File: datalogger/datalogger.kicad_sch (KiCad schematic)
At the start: 42 parts, among them J1 MSD-1-A, J2 USB4216-03-A_REVA, Q1 NPN, Q2 NPN, U1 BME280, U2 CP2102N-Axx-xQFN28, U3 ESP32-C3-MINI-1-N4, U4 TLV76133DCYR

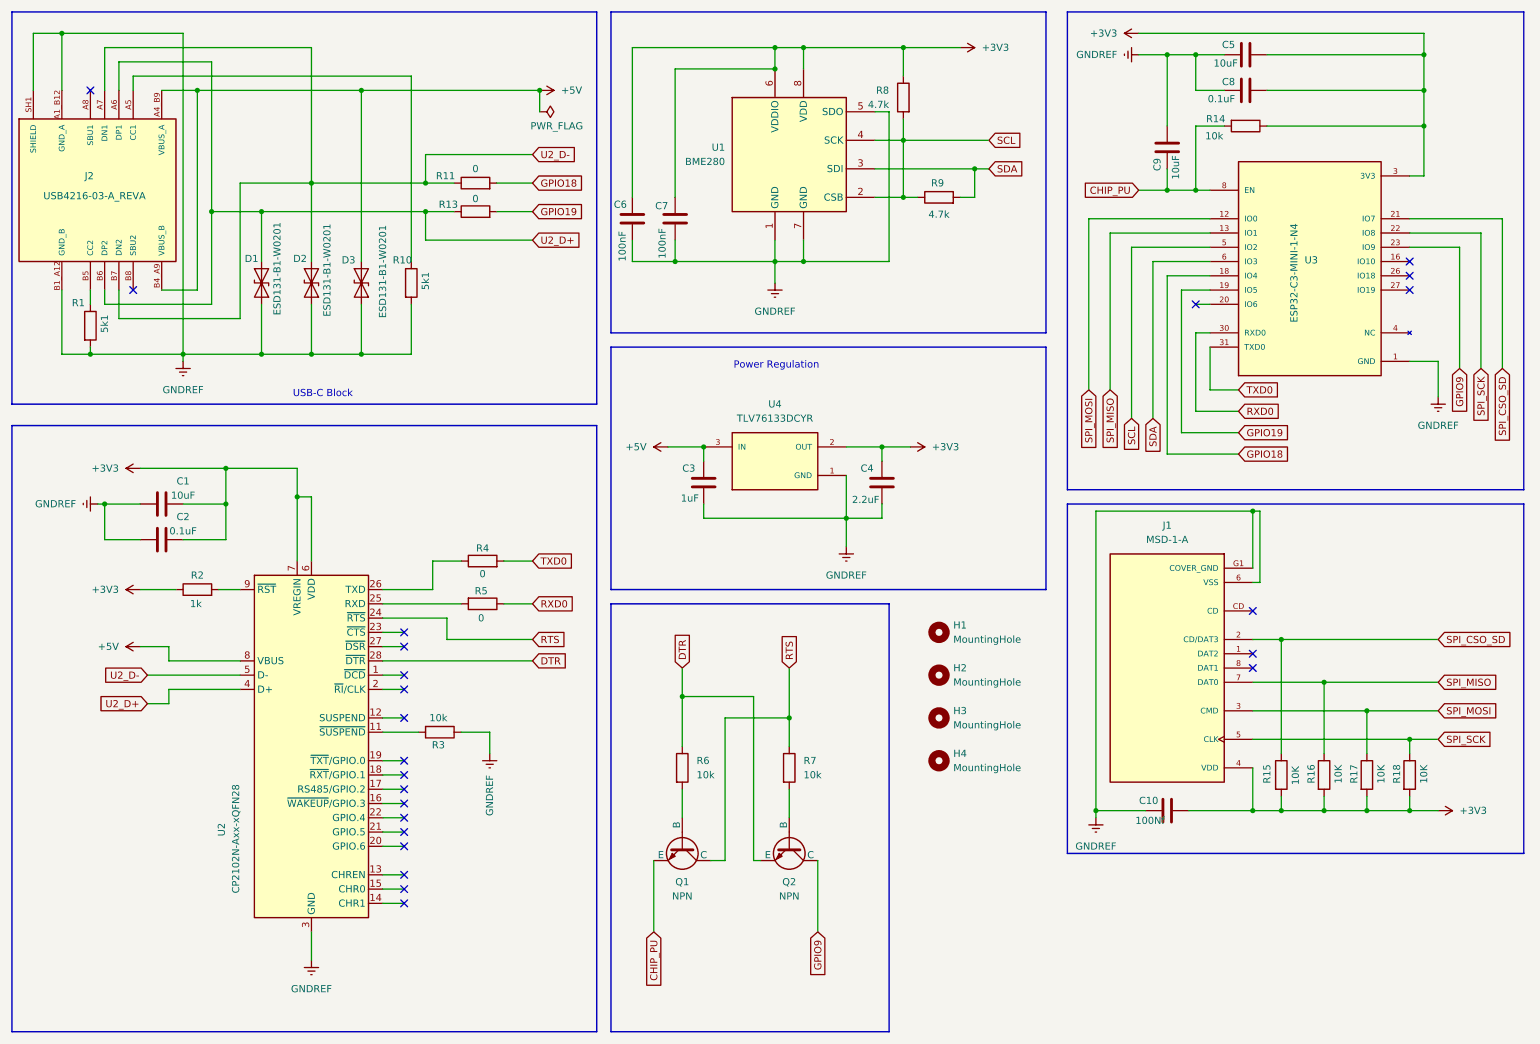
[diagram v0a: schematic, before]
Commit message: Change USB-C orientation
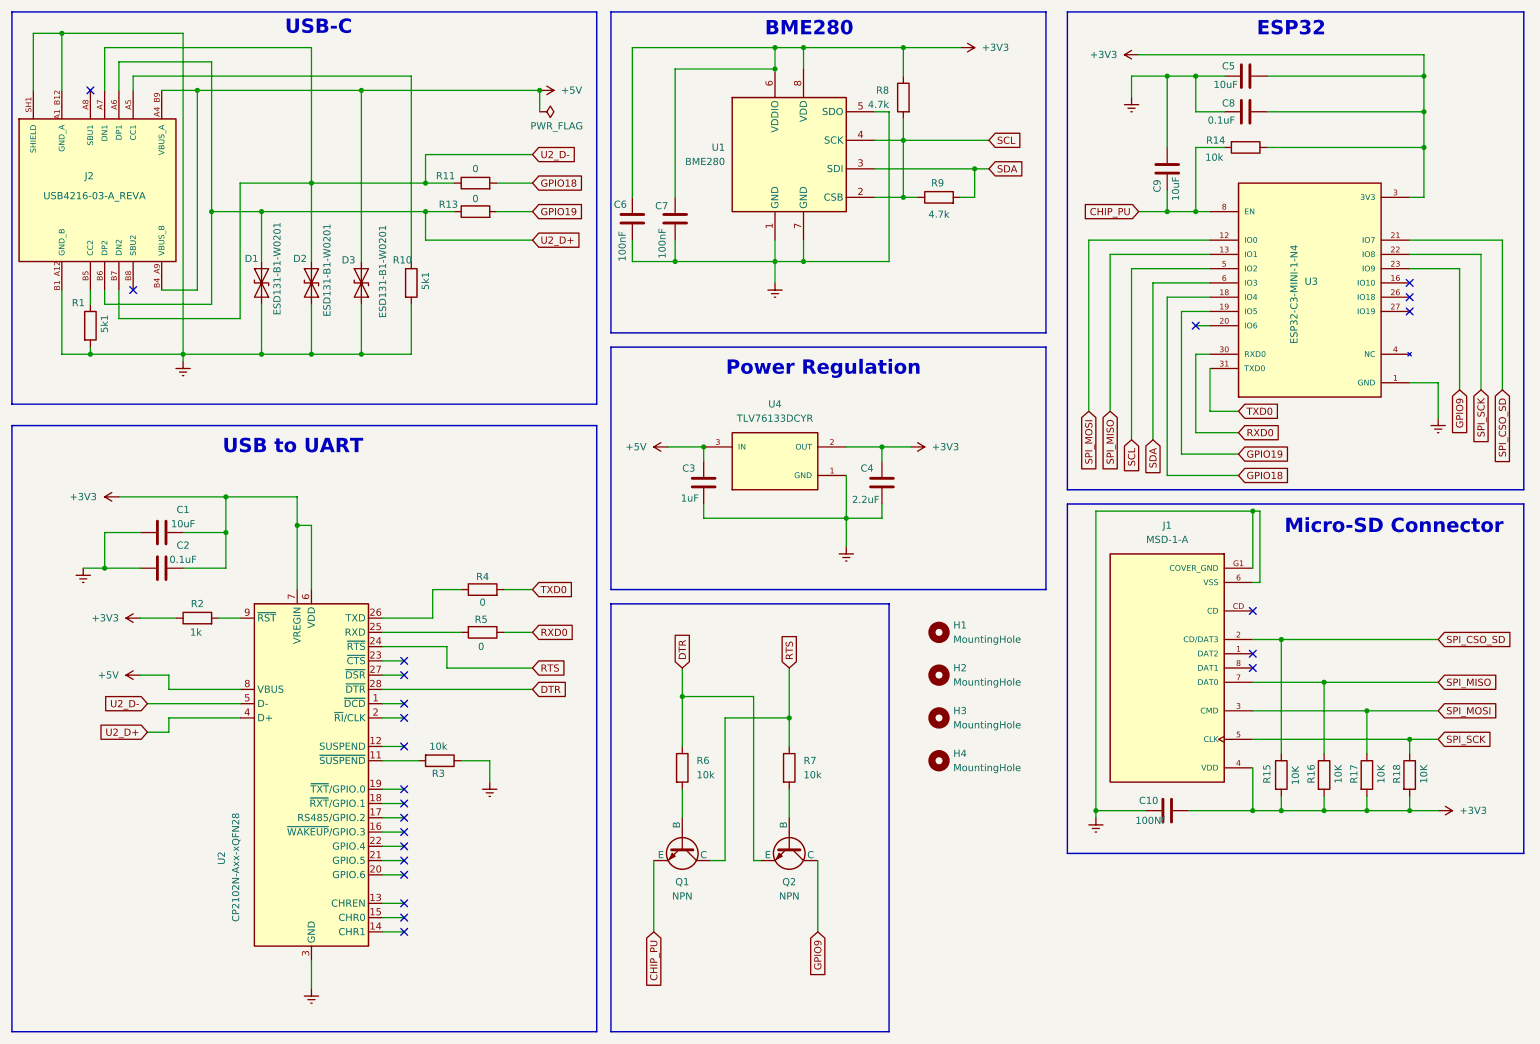
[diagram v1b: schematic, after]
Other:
- note added: "BME280"
- note added: "ESP32"
- note added: "Micro-SD Connector"
- note added: "USB to UART"
- note added: "USB-C"
- note removed: "USB-C Block"
- moved on the sheet: C1, C2, C5, C8, C9, R14, R2, R3, R4, R5, U2, U3
